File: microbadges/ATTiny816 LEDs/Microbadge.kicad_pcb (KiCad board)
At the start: 2 copper layers, 7 x 7 mm, 15 parts, among them U1 ATtiny816-M

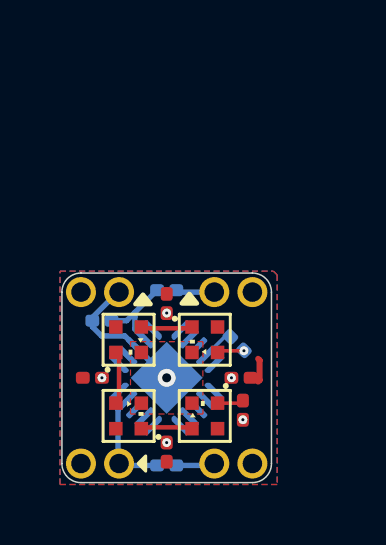
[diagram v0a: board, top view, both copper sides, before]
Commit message: Update ATTiny Voltage to use +VBATT instead of +3V3
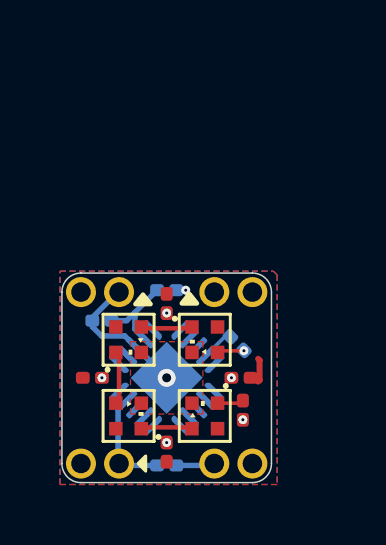
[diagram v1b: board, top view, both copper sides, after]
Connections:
- net /D_+3.3V renamed /D_+VBATT
- D1 pad 2: +3.3V -> +VBATT
- R1 pad 1: +3.3V -> +VBATT
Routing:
- net +3.3V: track 2.59 -> 1.29 mm
- net +VBATT: track 0.80 -> 1.12 mm, vias 0 -> 1
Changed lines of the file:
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@@
 	(net 1 "unconnected-(U1-PC1-Pad16)")
 	(net 2 "unconnected-(U1-PB2-Pad12)")
-	(net 3 "/D_+3.3V")
+	(net 3 "/D_+VBATT")
 	(net 4 "UPDI_PROG")
 	(net 5 "unconnected-(U1-PB1-Pad13)")
@@
 			(layers "B.Cu" "B.Mask")
 			(roundrect_rratio 0.25)
-			(net 20 "+3.3V")
+			(net 22 "+VBATT")
 			(pintype "passive")
 		)
@@
 			(layers "B.Cu" "B.Mask" "B.Paste")
 			(roundrect_rratio 0.25)
-			(net 3 "/D_+3.3V")
+			(net 3 "/D_+VBATT")
 			(pinfunction "VCC")
 			(pintype "power_in")
@@
 			(layers "B.Cu" "B.Mask")
 			(roundrect_rratio 0.25)
-			(net 3 "/D_+3.3V")
+			(net 3 "/D_+VBATT")
 			(pintype "passive")
 		)
@@
 			(layers "B.Cu" "B.Mask")
 			(roundrect_rratio 0.25)
-			(net 3 "/D_+3.3V")
+			(net 3 "/D_+VBATT")
 			(pinfunction "K")
 			(pintype "passive")
@@
 			(layers "B.Cu" "B.Mask")
 			(roundrect_rratio 0.25)
-			(net 20 "+3.3V")
+			(net 22 "+VBATT")
 			(pinfunction "A")
 			(pintype "passive")
@@
 	)
 	(segment
-		(start 148.0845 104.7115)
-		(end 148.021 104.648)
-		(width 0.18)
-		(layer "B.Cu")
-		(net 20)
-	)
-	(segment
 		(start 148.021 110.49)
 		(end 149.225 110.49)
@@
 	)
 	(segment
-		(start 149.2885 104.7115)
-		(end 148.0845 104.7115)
-		(width 0.18)
-		(layer "B.Cu")
-		(net 20)
-	)
-	(segment
 		(start 150.7985 107.6465)
 		(end 150.7985 106.9835)
@@
 		(net 22)
 	)
+	(via micro
+		(at 148.336 104.648)
+		(size 0.3)
+		(drill 0.1)
+		(layers "F.Cu" "B.Cu")
+		(net 22)
+	)
+	(segment
+		(start 148.021 104.648)
+		(end 148.336 104.648)
+		(width 0.2)
+		(layer "B.Cu")
+		(net 22)
+	)

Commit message: Update Microbadge to V2 design
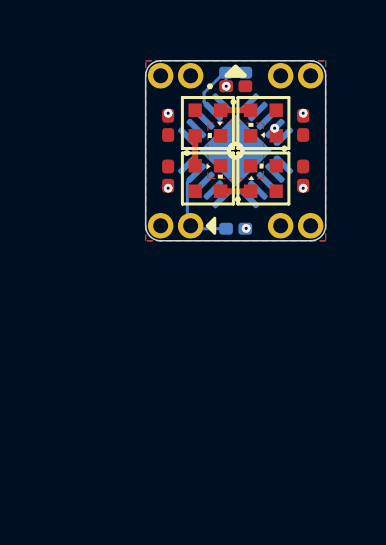
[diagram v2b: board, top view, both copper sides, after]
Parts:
- removed R2, R3: 500, Resistor_SMD:R_0201_0603Metric
- D1: moved to F.Cu
- MCB1: footprint Microbadge:Microbadge_round -> Microbadge V2:Microbadge_V2_simple_round
- moved C1 9.39 mm to (150.0, 97.4), turned to 180 degrees
- moved C3 9.20 mm to (147.8, 100.8), turned to -90 degrees
- moved C5 8.78 mm to (147.8, 99.2), turned to 90 degrees
- moved C4 8.67 mm to (152.2, 99.2), turned to 90 degrees
- moved D4 8.34 mm to (149.1, 100.9)
- moved R1 8.22 mm to (150.0, 102.6)
- moved D5 8.15 mm to (150.9, 100.9)
- moved MCB1 7.91 mm to (150.0, 100.0)
- moved U1 7.91 mm to (150.0, 100.0)
- moved D3 7.69 mm to (149.1, 99.1)
- moved D2 7.48 mm to (150.9, 99.1)
- moved D1 7.18 mm to (150.0, 97.8)
- moved C2 6.22 mm to (152.2, 100.8)
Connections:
- D2 pad 4: Net-(D2-DIN) -> LED
- D5 pad 1: Net-(D5-DOUT) -> unconnected-(D5-DOUT-Pad1)
- MCB1 pad 5: CLK -> unconnected-(MCB1-+3V3-Pad5)
- MCB1 pad 6: UPDI_PROG -> GND
- MCB1 pad 7: +3.3V -> CLK
- MCB1 pad 8: GND -> UPDI_PROG
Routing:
- net GND: track 4.74 -> 0.34 mm, vias 6 -> 5
- net +3.3V: track 1.29 -> 0.00 mm
- net LED: track 1.07 -> 0.00 mm, vias 0 -> 1
- net +VBATT: track 1.12 -> 0.09 mm
- net Net-(D2-DIN): track 0.92 -> 0.00 mm, vias 1 -> 0
- net Net-(D5-DOUT): track 0.88 -> 0.00 mm
- net Net-(D3-DOUT): track 1.75 -> 1.00 mm
- net /D_+VBATT: track 2.94 -> 2.21 mm, vias 0 -> 1
- net Net-(D4-DOUT): track 1.70 -> 1.00 mm
- net Net-(D2-DOUT): track 1.70 -> 1.00 mm
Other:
- board size 7 x 7 mm -> 6 x 6 mm
